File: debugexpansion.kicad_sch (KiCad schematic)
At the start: 0 parts

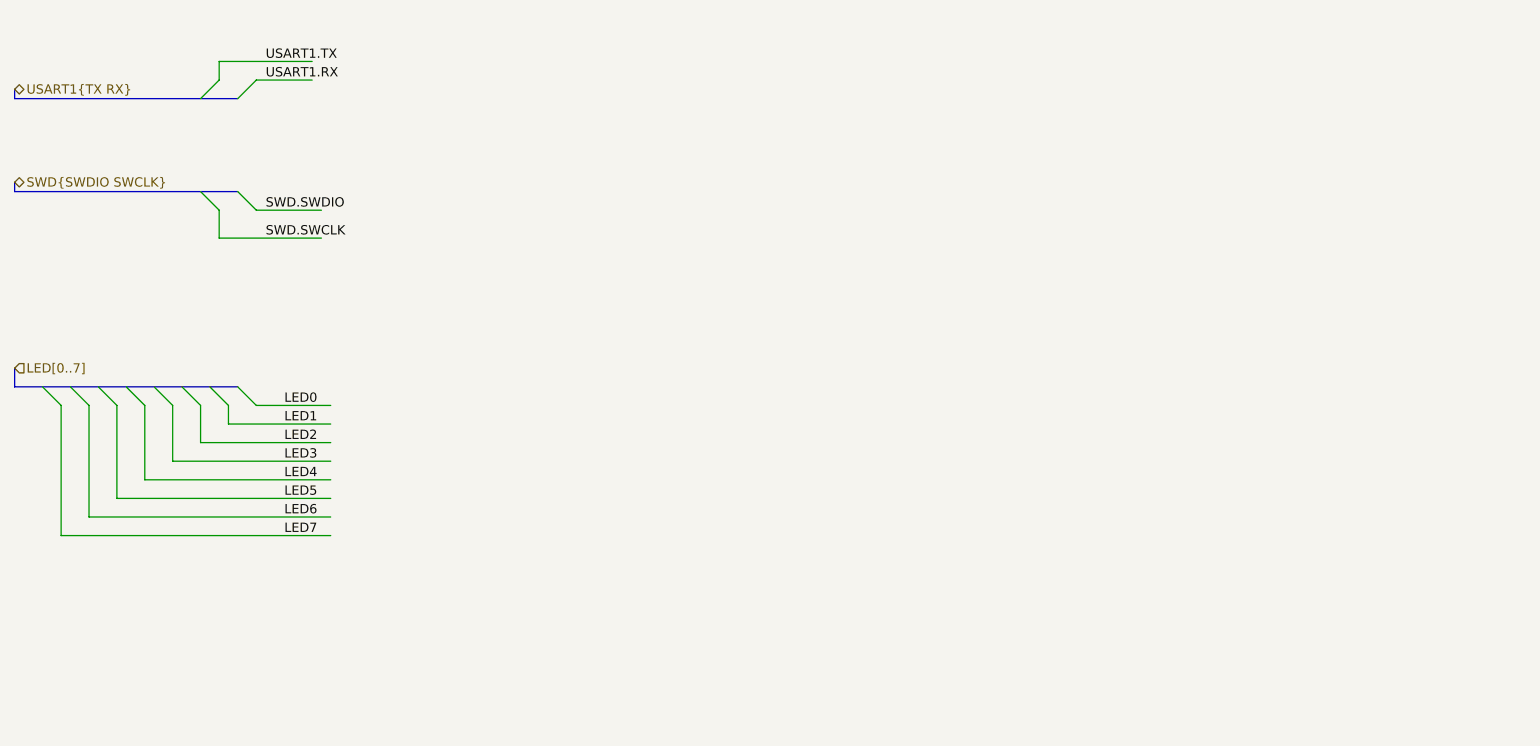
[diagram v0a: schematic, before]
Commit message: Update debugexpansion.kicad_sch
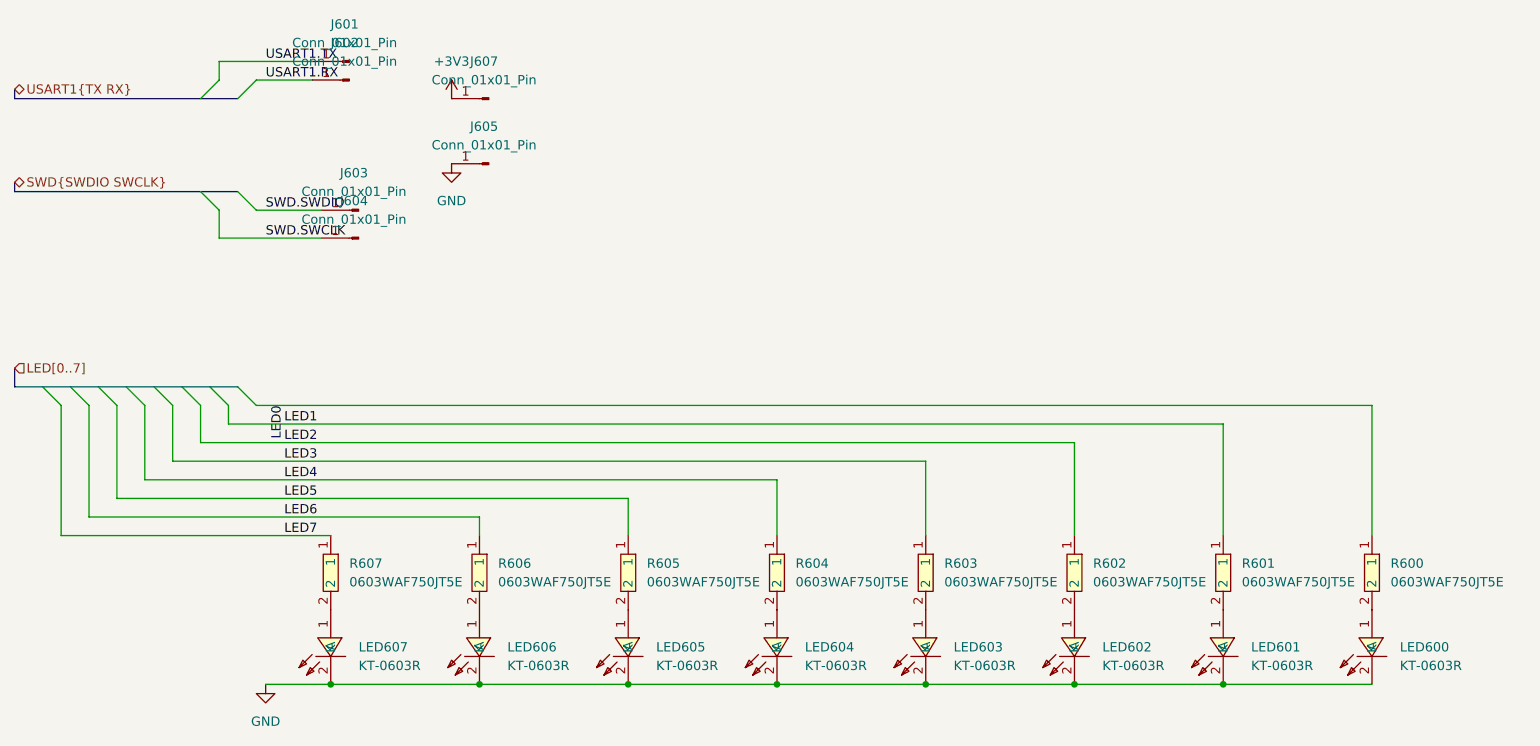
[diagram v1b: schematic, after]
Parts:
- added J601, J602, J603, J604, J605, J607: Conn_01x01_Pin, symbol Connector:Conn_01x01_Pin
- added LED600, LED601, LED602, LED603, LED604, LED605, LED606, LED607: KT-0603R, EasyEDA:LED-SMD_L1.6-W0.8-R-RD, symbol EasyEDA:KT-0603R
- added R600, R601, R602, R603, R604, R605, R606, R607: 0603WAF750JT5E, EasyEDA:R0603, symbol EasyEDA:0603WAF750JT5E
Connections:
- net LED0: now also R600.1
- net LED1: now also R601.1
- net LED2: now also R602.1
- net LED3: now also R603.1
- net LED4: now also R604.1
- net LED5: now also R605.1
- net LED6: now also R606.1
- net LED7: now also R607.1
- net SWD.SWCLK: now also J604.1 (Pin_1)
- net SWD.SWDIO: now also J603.1 (Pin_1)
- net USART1.RX: now also J602.1 (Pin_1)
- net USART1.TX: now also J601.1 (Pin_1)
- new net: LED606.1 (A), R606.2
- new net: LED605.1 (A), R605.2
- new net: LED603.1 (A), R603.2
- new net: LED607.1 (A), R607.2
- new net: LED604.1 (A), R604.2
- new net: LED602.1 (A), R602.2
- new net: LED601.1 (A), R601.2
- new net: LED600.1 (A), R600.2
- new net +3V3: J607.1 (Pin_1)
- new net GND: J605.1 (Pin_1), LED600.2 (K), LED601.2 (K), LED602.2 (K), LED603.2 (K), LED604.2 (K), LED605.2 (K), LED606.2 (K), LED607.2 (K)
